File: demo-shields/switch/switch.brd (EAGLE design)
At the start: 68.6 x 53.3 mm, 18 parts, among them J4 J5MM, T1 2N2222

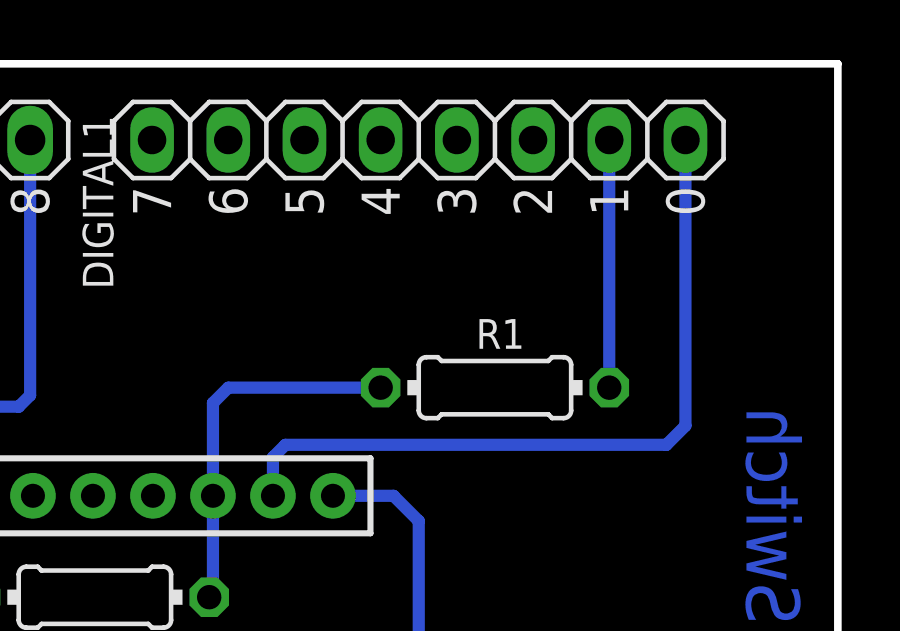
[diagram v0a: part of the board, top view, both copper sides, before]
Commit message: fix: Use software serial for WiFly communication
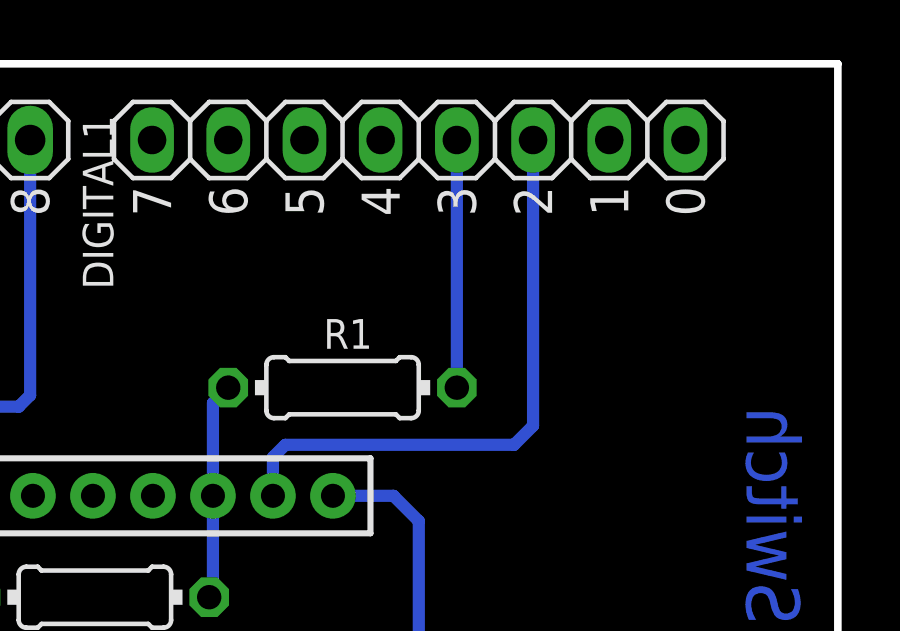
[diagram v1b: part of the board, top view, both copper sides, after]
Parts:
- moved R1 5.08 mm to (52.1, 42.5)
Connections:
- net RXD: now also DIGITAL1.3; no longer DIGITAL1.1
- net TXD: now also DIGITAL1.4; no longer DIGITAL1.2
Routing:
- net N$1: track 12.3 -> 7.25 mm
- net RXD: track 25.0 -> 19.9 mm
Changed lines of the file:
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@@
 <attribute name="VALUE" x="33.02" y="36.83" size="0.4064" layer="27" rot="R270"/>
 </element>
-<element name="R1" library="rcl" package="0204/7" value="1k5" x="57.15" y="42.545" smashed="yes">
-<attribute name="NAME" x="56.515" y="43.8404" size="0.9906" layer="25" ratio="10"/>
-<attribute name="VALUE" x="55.5244" y="42.0624" size="0.9906" layer="27" ratio="10"/>
+<element name="R1" library="rcl" package="0204/7" value="1k5" x="52.07" y="42.545" smashed="yes">
+<attribute name="NAME" x="51.435" y="43.8404" size="0.9906" layer="25" ratio="10"/>
+<attribute name="VALUE" x="50.4444" y="42.0624" size="0.9906" layer="27" ratio="10"/>
 </element>
 <element name="R2" library="rcl" package="0204/7" value="3k" x="43.815" y="35.56" smashed="yes">
@@
 <signals>
 <signal name="RXD">
-<contactref element="DIGITAL1" pad="1"/>
 <contactref element="WIFLY" pad="2"/>
-<wire x1="63.5" y1="41.275" x2="62.865" y2="40.64" width="0.4064" layer="16"/>
 <wire x1="49.75" y1="38.94" x2="49.75" y2="40.225" width="0.4064" layer="16"/>
 <wire x1="49.75" y1="40.225" x2="50.165" y2="40.64" width="0.4064" layer="16"/>
-<wire x1="50.165" y1="40.64" x2="62.865" y2="40.64" width="0.4064" layer="16"/>
-<wire x1="63.5" y1="41.275" x2="63.5" y2="50.8" width="0.4064" layer="16"/>
+<contactref element="DIGITAL1" pad="3"/>
+<wire x1="50.165" y1="40.64" x2="57.785" y2="40.64" width="0.4064" layer="16"/>
+<wire x1="57.785" y1="40.64" x2="58.42" y2="41.275" width="0.4064" layer="16"/>
+<wire x1="58.42" y1="41.275" x2="58.42" y2="50.8" width="0.4064" layer="16"/>
 </signal>
 <signal name="GND">
@@
 </signal>
 <signal name="TXD">
-<contactref element="DIGITAL1" pad="2"/>
 <contactref element="R1" pad="2"/>
-<wire x1="60.96" y1="50.8" x2="60.96" y2="42.545" width="0.4064" layer="16"/>
+<contactref element="DIGITAL1" pad="4"/>
+<wire x1="55.88" y1="50.8" x2="55.88" y2="42.545" width="0.4064" layer="16"/>
 </signal>
 <signal name="+5V">
@@
 <contactref element="R1" pad="1"/>
 <contactref element="R2" pad="2"/>
-<wire x1="47.75" y1="42.035" x2="48.26" y2="42.545" width="0.4064" layer="16"/>
 <wire x1="47.75" y1="38.94" x2="47.75" y2="35.685" width="0.4064" layer="16"/>
 <wire x1="47.75" y1="35.685" x2="47.625" y2="35.56" width="0.4064" layer="16"/>
 <wire x1="47.75" y1="38.94" x2="47.75" y2="42.035" width="0.4064" layer="16"/>
-<wire x1="48.26" y1="42.545" x2="53.34" y2="42.545" width="0.4064" layer="16"/>
+<wire x1="47.75" y1="42.035" x2="48.26" y2="42.545" width="0.4064" layer="16"/>
 </signal>
 <signal name="N$2">
